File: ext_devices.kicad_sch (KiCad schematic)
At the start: 12 parts, among them CON1 MIKROBUS_HOST_CONN, J10 Conn_01x08_Female, J9 Conn_01x08_Female, U14 TXS0102DCU, U15 TXS0102DCU

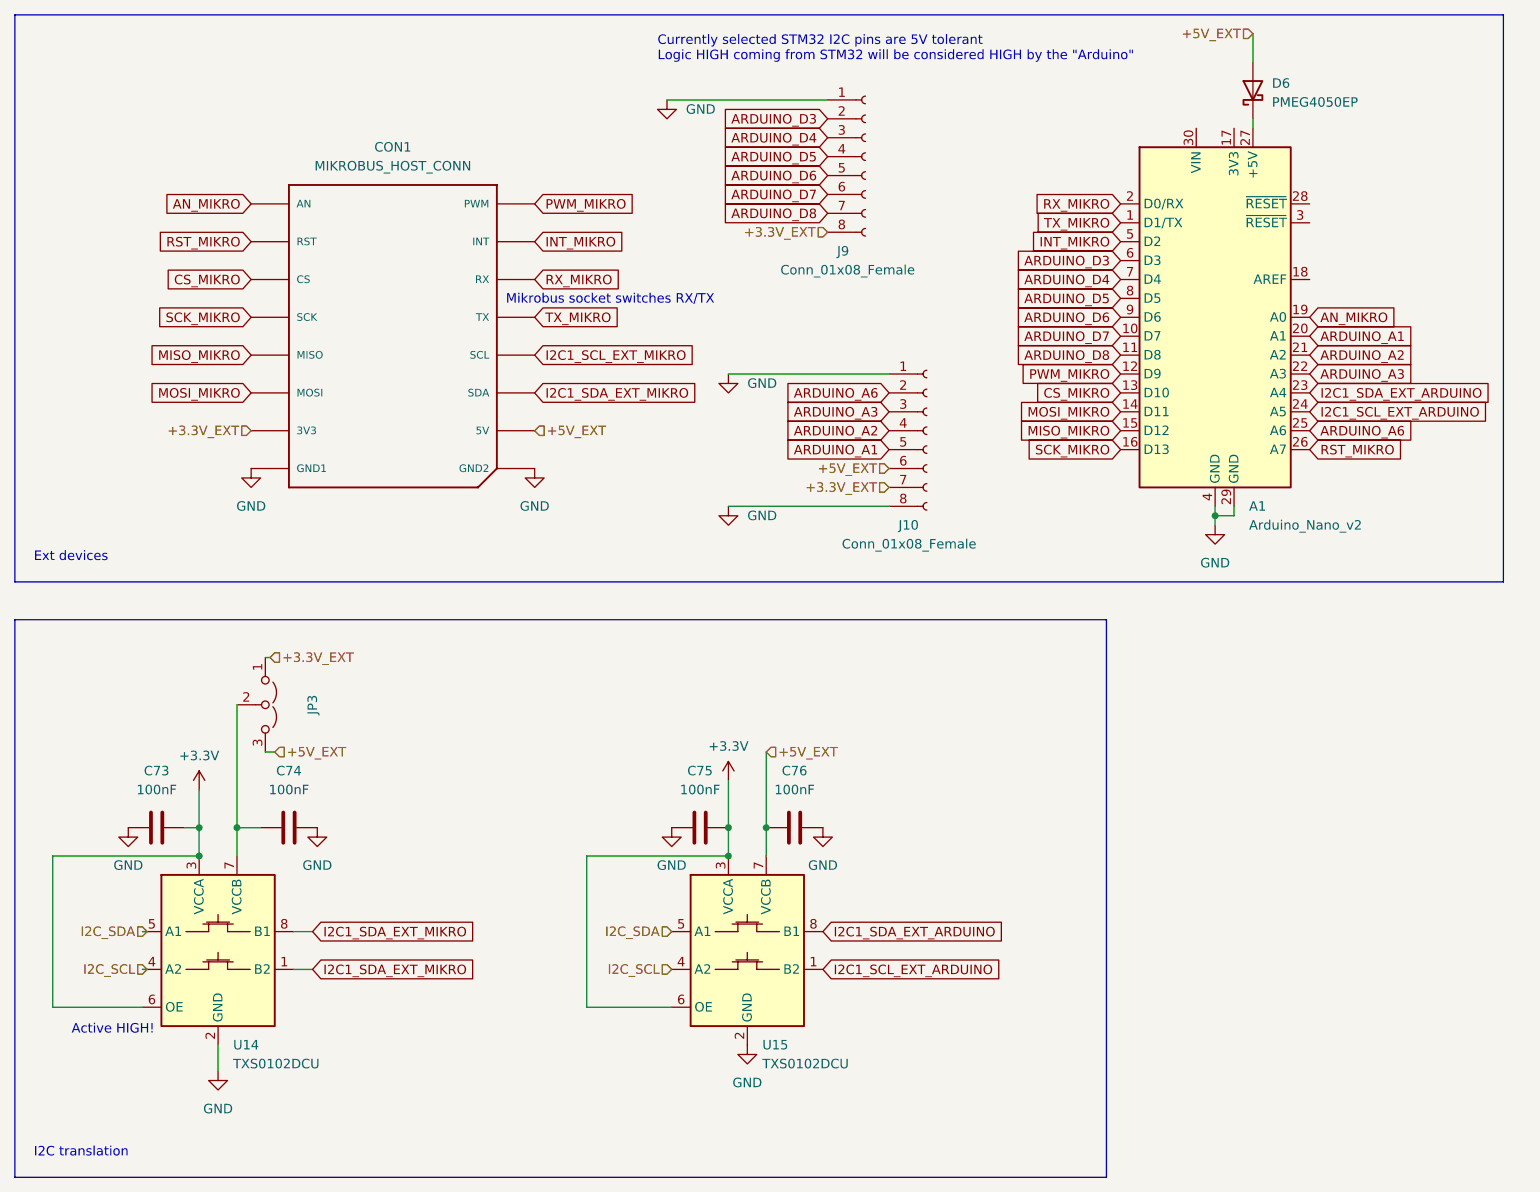
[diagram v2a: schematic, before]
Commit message: replaced main MCU, reannotated
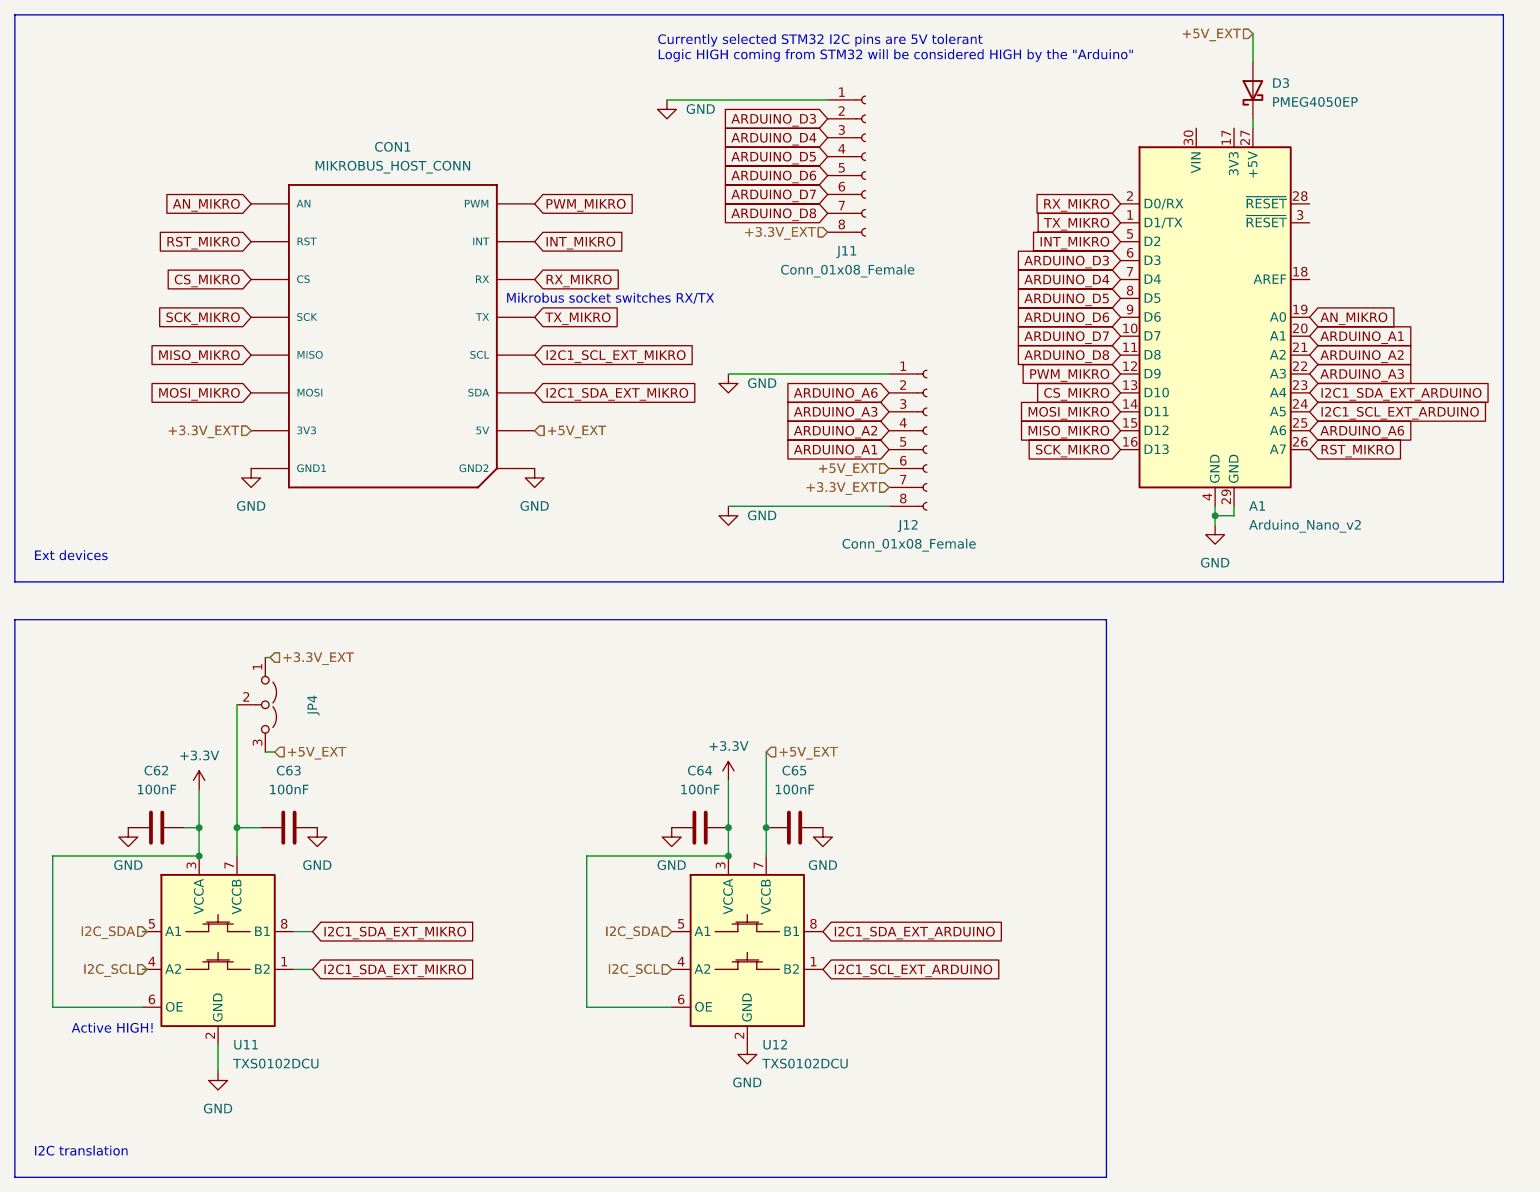
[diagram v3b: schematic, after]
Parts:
- renumbered C73 to C62, C74 to C63, C75 to C64, C76 to C65, D6 to D3, J9 to J11, J10 to J12, JP3 to JP4, U14 to U11, U15 to U12
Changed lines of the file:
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@@
   (symbol (lib_id "power:GND") (at 124.46 165.1 0) (unit 1)
     (in_bom yes) (on_board yes) (fields_autoplaced)
-    (property "Reference" "#PWR0191" (id 0) (at 124.46 171.45 0)
+    (property "Reference" "#PWR095" (id 0) (at 124.46 171.45 0)
       (effects (font (size 1.27 1.27)) hide)
     )
@@
   (symbol (lib_id "power:+3.3V") (at 50.8 130.81 0) (unit 1)
     (in_bom yes) (on_board yes) (fields_autoplaced)
-    (property "Reference" "#PWR0178" (id 0) (at 50.8 134.62 0)
+    (property "Reference" "#PWR090" (id 0) (at 50.8 134.62 0)
       (effects (font (size 1.27 1.27)) hide)
     )
@@
   (symbol (lib_id "Jumper:Jumper_3_Open") (at 59.69 119.38 270) (unit 1)
     (in_bom yes) (on_board yes)
-    (property "Reference" "JP3" (id 0) (at 66.04 119.38 0))
+    (property "Reference" "JP4" (id 0) (at 66.04 119.38 0))
     (property "Value" " " (id 1) (at 63.5 119.38 0))
     (property "Footprint" "Connector_PinHeader_2.54mm:PinHeader_1x03_P2.54mm_Vertical" (id 2) (at 59.69 119.38 0)
@@
   (symbol (lib_id "power:GND") (at 187.325 95.25 0) (unit 1)
     (in_bom yes) (on_board yes) (fields_autoplaced)
-    (property "Reference" "#PWR0176" (id 0) (at 187.325 101.6 0)
+    (property "Reference" "#PWR088" (id 0) (at 187.325 101.6 0)
       (effects (font (size 1.27 1.27)) hide)
     )
@@
   (symbol (lib_id "power:GND") (at 134.62 135.89 0) (unit 1)
     (in_bom yes) (on_board yes) (fields_autoplaced)
-    (property "Reference" "#PWR0192" (id 0) (at 134.62 142.24 0)
+    (property "Reference" "#PWR094" (id 0) (at 134.62 142.24 0)
       (effects (font (size 1.27 1.27)) hide)
     )
@@
   (symbol (lib_id "Device:C") (at 130.81 135.89 90) (unit 1)
     (in_bom yes) (on_board yes) (fields_autoplaced)
-    (property "Reference" "C76" (id 0) (at 130.81 128.27 90))
+    (property "Reference" "C65" (id 0) (at 130.81 128.27 90))
     (property "Value" "100nF" (id 1) (at 130.81 130.81 90))
     (property "Footprint" "Capacitor_SMD:C_0805_2012Metric_Pad1.18x1.45mm_HandSolder" (id 2) (at 134.62 134.9248 0)
@@
   (symbol (lib_id "power:GND") (at 57.785 87.63 0) (unit 1)
     (in_bom yes) (on_board yes) (fields_autoplaced)
-    (property "Reference" "#PWR0185" (id 0) (at 57.785 93.98 0)
+    (property "Reference" "#PWR085" (id 0) (at 57.785 93.98 0)
       (effects (font (size 1.27 1.27)) hide)
     )
@@
   (symbol (lib_id "power:GND") (at 41.275 135.89 0) (unit 1)
     (in_bom yes) (on_board yes) (fields_autoplaced)
-    (property "Reference" "#PWR0179" (id 0) (at 41.275 142.24 0)
+    (property "Reference" "#PWR091" (id 0) (at 41.275 142.24 0)
       (effects (font (size 1.27 1.27)) hide)
     )
@@
   (symbol (lib_id "Device:C") (at 118.11 135.89 90) (unit 1)
     (in_bom yes) (on_board yes) (fields_autoplaced)
-    (property "Reference" "C75" (id 0) (at 118.11 128.27 90))
+    (property "Reference" "C64" (id 0) (at 118.11 128.27 90))
     (property "Value" "100nF" (id 1) (at 118.11 130.81 90))
     (property "Footprint" "Capacitor_SMD:C_0805_2012Metric_Pad1.18x1.45mm_HandSolder" (id 2) (at 121.92 134.9248 0)
@@
   (symbol (lib_id "power:GND") (at 53.3378 168.6027 0) (unit 1)
     (in_bom yes) (on_board yes) (fields_autoplaced)
-    (property "Reference" "#PWR0180" (id 0) (at 53.3378 174.9527 0)
+    (property "Reference" "#PWR096" (id 0) (at 53.3378 174.9527 0)
       (effects (font (size 1.27 1.27)) hide)
     )
@@
   (symbol (lib_id "Device:C") (at 62.865 135.89 90) (unit 1)
     (in_bom yes) (on_board yes) (fields_autoplaced)
-    (property "Reference" "C74" (id 0) (at 62.865 128.27 90))
+    (property "Reference" "C63" (id 0) (at 62.865 128.27 90))
     (property "Value" "100nF" (id 1) (at 62.865 130.81 90))
     (property "Footprint" "Capacitor_SMD:C_0805_2012Metric_Pad1.18x1.45mm_HandSolder" (id 2) (at 66.675 134.9248 0)
@@
   (symbol (lib_id "power:GND") (at 113.665 38.1 0) (unit 1)
     (in_bom yes) (on_board yes) (fields_autoplaced)
-    (property "Reference" "#PWR0184" (id 0) (at 113.665 44.45 0)
+    (property "Reference" "#PWR083" (id 0) (at 113.665 44.45 0)
       (effects (font (size 1.27 1.27)) hide)
     )
@@
   (symbol (lib_id "power:GND") (at 66.675 135.89 0) (unit 1)
     (in_bom yes) (on_board yes) (fields_autoplaced)
-    (property "Reference" "#PWR0177" (id 0) (at 66.675 142.24 0)
+    (property "Reference" "#PWR092" (id 0) (at 66.675 142.24 0)
       (effects (font (size 1.27 1.27)) hide)
     )
@@
   (symbol (lib_id "power:GND") (at 95.885 87.63 0) (unit 1)
     (in_bom yes) (on_board yes) (fields_autoplaced)
-    (property "Reference" "#PWR0182" (id 0) (at 95.885 93.98 0)
+    (property "Reference" "#PWR086" (id 0) (at 95.885 93.98 0)
       (effects (font (size 1.27 1.27)) hide)
     )
@@
   (symbol (lib_id "Logic_LevelTranslator:TXS0102DCU") (at 124.46 152.4 0) (unit 1)
     (in_bom yes) (on_board yes) (fields_autoplaced)
-    (property "Reference" "U15" (id 0) (at 126.4794 165.1 0)
+    (property "Reference" "U12" (id 0) (at 126.4794 165.1 0)
       (effects (font (size 1.27 1.27)) (justify left))
     )
@@
   (symbol (lib_id "Connector:Conn_01x08_Female") (at 148.59 82.55 0) (unit 1)
     (in_bom yes) (on_board yes)
-    (property "Reference" "J10" (id 0) (at 144.78 95.25 0)
+    (property "Reference" "J12" (id 0) (at 144.78 95.25 0)
       (effects (font (size 1.27 1.27)) (justify left))
     )
@@
   (symbol (lib_id "power:GND") (at 121.92 92.71 0) (unit 1)
     (in_bom yes) (on_board yes) (fields_autoplaced)
-    (property "Reference" "#PWR0181" (id 0) (at 121.92 99.06 0)
+    (property "Reference" "#PWR087" (id 0) (at 121.92 99.06 0)
       (effects (font (size 1.27 1.27)) hide)
     )
@@
   (symbol (lib_id "Device:C") (at 45.085 135.89 90) (unit 1)
     (in_bom yes) (on_board yes) (fields_autoplaced)
-    (property "Reference" "C73" (id 0) (at 45.085 128.27 90))
+    (property "Reference" "C62" (id 0) (at 45.085 128.27 90))
     (property "Value" "100nF" (id 1) (at 45.085 130.81 90))
     (property "Footprint" "Capacitor_SMD:C_0805_2012Metric_Pad1.18x1.45mm_HandSolder" (id 2) (at 48.895 134.9248 0)
@@
   (symbol (lib_id "power:GND") (at 121.92 74.93 0) (unit 1)
     (in_bom yes) (on_board yes) (fields_autoplaced)
-    (property "Reference" "#PWR0183" (id 0) (at 121.92 81.28 0)
+    (property "Reference" "#PWR084" (id 0) (at 121.92 81.28 0)
       (effects (font (size 1.27 1.27)) hide)
     )
@@
   (symbol (lib_id "Connector:Conn_01x08_Female") (at 140.335 45.72 0) (unit 1)
     (in_bom yes) (on_board yes)
-    (property "Reference" "J9" (id 0) (at 136.525 58.42 0)
+    (property "Reference" "J11" (id 0) (at 136.525 58.42 0)
       (effects (font (size 1.27 1.27)) (justify left))
     )
@@
   (symbol (lib_id "Device:D_Schottky") (at 192.405 36.83 90) (unit 1)
     (in_bom yes) (on_board yes) (fields_autoplaced)
-    (property "Reference" "D6" (id 0) (at 194.945 35.8774 90)
+    (property "Reference" "D3" (id 0) (at 194.945 35.8774 90)
       (effects (font (size 1.27 1.27)) (justify right))
     )
@@
   (symbol (lib_id "power:GND") (at 114.3 135.89 0) (unit 1)
     (in_bom yes) (on_board yes) (fields_autoplaced)
-    (property "Reference" "#PWR0190" (id 0) (at 114.3 142.24 0)
+    (property "Reference" "#PWR093" (id 0) (at 114.3 142.24 0)
       (effects (font (size 1.27 1.27)) hide)
     )
@@
   (symbol (lib_id "Logic_LevelTranslator:TXS0102DCU") (at 53.34 152.4 0) (unit 1)
     (in_bom yes) (on_board yes) (fields_autoplaced)
-    (property "Reference" "U14" (id 0) (at 55.3594 165.1 0)
+    (property "Reference" "U11" (id 0) (at 55.3594 165.1 0)
       (effects (font (size 1.27 1.27)) (justify left))
     )
@@
   (symbol (lib_id "power:+3.3V") (at 121.92 129.54 0) (unit 1)
     (in_bom yes) (on_board yes) (fields_autoplaced)
-    (property "Reference" "#PWR0193" (id 0) (at 121.92 133.35 0)
-      (effects (font (size 1.27 1.27)) hide)
-    )
+    (property "Reference" "#PWR089" (id 0) (at 121.92 133.35 0)
+      (effects (font (size 1.27 1.27)) hide)
+    )

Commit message: resolved all erc errors
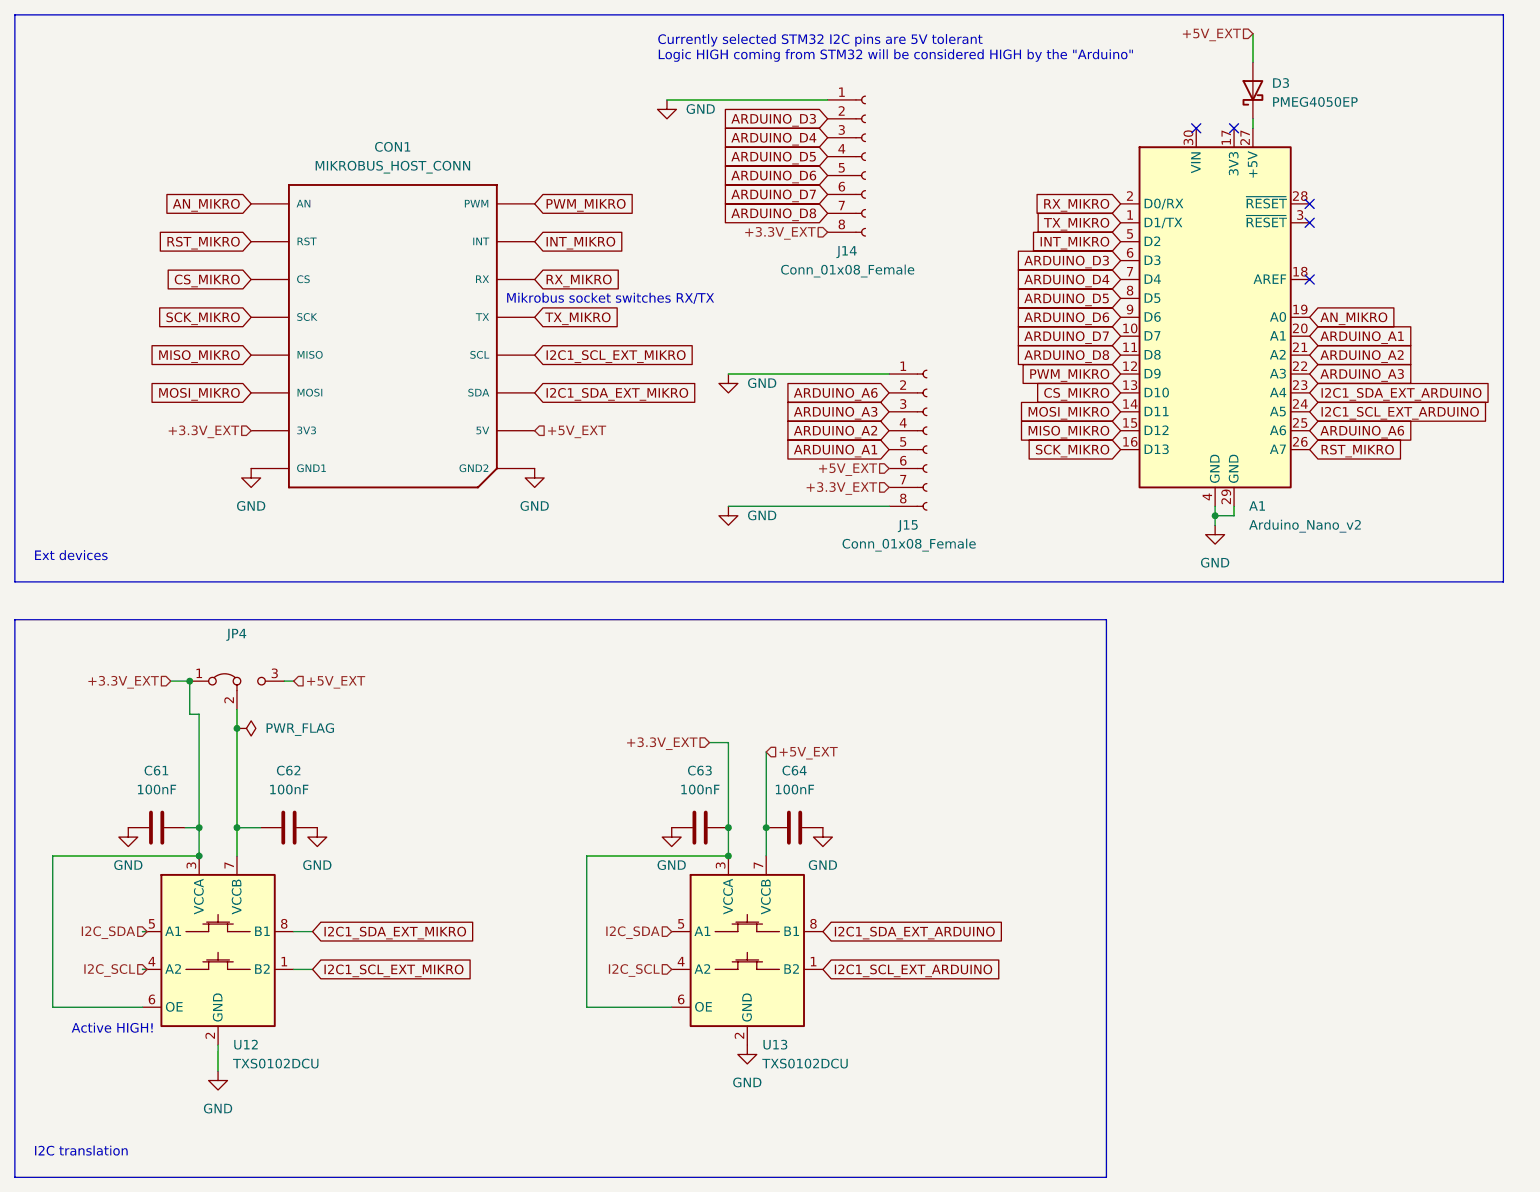
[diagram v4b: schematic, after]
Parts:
- JP4: symbol Jumper:Jumper_3_Open -> Jumper:Jumper_3_Bridged12
- renumbered C62 to C61, C63 to C62, C64 to C63, C65 to C64, J11 to J14, J12 to J15, U11 to U12, U12 to U13
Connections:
- net +3V3 is gone; now on net +3.3V_EXT: C61.2, C63.2, U12.3 (VCCA), U12.6 (OE), U13.3 (VCCA), U13.6 (OE)
- net I2C1_SCL_EXT_MIKRO: now also U12.1 (B2)
- net I2C1_SDA_EXT_MIKRO: no longer U12.1 (B2)
- no-connect marks 0 -> 5

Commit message: updated footprints from schematics
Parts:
- C61, C62, C63, C64: LCSC (none) -> C49678
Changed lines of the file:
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@@
       (effects (font (size 1.27 1.27)) hide)
     )
-    (property "Datasheet" "~" (id 3) (at 130.81 135.89 0)
+    (property "Datasheet" "https://datasheet.lcsc.com/lcsc/1810101813_YAGEO-CC0805KRX7R9BB104_C49678.pdf" (id 3) (at 130.81 135.89 0)
+      (effects (font (size 1.27 1.27)) hide)
+    )
+    (property "LCSC" "C49678" (id 4) (at 130.81 135.89 0)
       (effects (font (size 1.27 1.27)) hide)
     )
@@
       (effects (font (size 1.27 1.27)) hide)
     )
-    (property "Datasheet" "~" (id 3) (at 118.11 135.89 0)
+    (property "Datasheet" "https://datasheet.lcsc.com/lcsc/1810101813_YAGEO-CC0805KRX7R9BB104_C49678.pdf" (id 3) (at 118.11 135.89 0)
+      (effects (font (size 1.27 1.27)) hide)
+    )
+    (property "LCSC" "C49678" (id 4) (at 118.11 135.89 0)
       (effects (font (size 1.27 1.27)) hide)
     )
@@
       (effects (font (size 1.27 1.27)) hide)
     )
-    (property "Datasheet" "~" (id 3) (at 62.865 135.89 0)
+    (property "Datasheet" "https://datasheet.lcsc.com/lcsc/1810101813_YAGEO-CC0805KRX7R9BB104_C49678.pdf" (id 3) (at 62.865 135.89 0)
+      (effects (font (size 1.27 1.27)) hide)
+    )
+    (property "LCSC" "C49678" (id 4) (at 62.865 135.89 0)
       (effects (font (size 1.27 1.27)) hide)
     )
@@
       (effects (font (size 1.27 1.27)) hide)
     )
-    (property "Datasheet" "~" (id 3) (at 45.085 135.89 0)
-      (effects (font (size 1.27 1.27)) hide)
-    )
+    (property "Datasheet" "https://datasheet.lcsc.com/lcsc/1810101813_YAGEO-CC0805KRX7R9BB104_C49678.pdf" (id 3) (at 45.085 135.89 0)
+      (effects (font (size 1.27 1.27)) hide)
+    )
+    (property "LCSC" "C49678" (id 4) (at 45.085 135.89 0)
+      (effects (font (size 1.27 1.27)) hide)
+    )
